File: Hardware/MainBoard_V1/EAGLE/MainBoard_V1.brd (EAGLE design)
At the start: 85 x 50 mm, 25 parts, among them IC1 REG1117, J1 NANO_FOOTPRINTNANO, J4 I2C, K1 RELAY-SPDT-JZC-11F, Q2 600mA/40V, Q3 600mA/40V, U1 MOC3021M, U2 TXB0104, U4 MCT2EM, X2 AC

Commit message: SubBoard_V1 initial state
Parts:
- removed U2: TXB0104, SparkFun-IC-Comms:SO14
- added JP1: (no value), SparkFun-Jumpers:SMT-JUMPER_2_NO_SILK
- added U$1, U$2, U$3, U$4, U$5, U$6, U$7, U$8: FIDUCIAL, adafruit:FIDUCIAL_1MM
- added U3: (no value), adafruit:VFSOP-8
- D2: value 1A/50V/1.1V -> S1M; device SparkFun-DiscreteSemi:DIODE-1N4001 -> diode:SMA
- R1, R3, R4, R5, R6: device rcl:R0402 -> rcl:R0603
- moved R6 9.27 mm to (34.0, 47.1)
- moved Q3 8.00 mm to (37.0, 46.0)
- moved Q2 7.52 mm to (37.0, 47.0)
- moved D2 5.71 mm to (43.7, 47.2), turned to 180 degrees
- moved R5 3.50 mm to (39.5, 45.9), turned to 270 degrees
- moved R4 2.43 mm to (31.9, 37.0), flipped to the bottom, turned to 90 degrees
- moved R1 1.26 mm to (68.0, 38.0)
- moved R3 1.14 mm to (34.0, 37.0), turned to 90 degrees
- moved C1 1.08 mm to (53.0, 32.0)
- moved K1 1.00 mm to (58.0, 43.5)
- moved U1 0.40 mm to (40.0, 38.5)
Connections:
- net 3V3: now also U3.P$3, U3.P$6; no longer U2.1, U2.8
- net 5V: now also JP1.2, U3.P$7; no longer U2.14
- net A4: now also U3.P$1; no longer U2.11
- net A5: now also U3.P$8; no longer U2.10
- net GND: now also U3.P$2; no longer U2.7
- net SCL: now also U3.P$5; no longer U2.5
- net SDA: now also U3.P$4; no longer U2.4
- net VIN: now also JP1.1
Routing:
- net GND: track 168.1 -> 122.3 mm, vias 2 -> 16
- net D9: track 50.3 -> 58.0 mm
- net SDA: track 30.5 -> 24.1 mm
- net PUMP: track 73.5 -> 79.9 mm
- net 5V: track 56.8 -> 51.0 mm
- net N$9: track 22.9 -> 17.4 mm, vias 0 -> 1
- net D10: track 65.3 -> 60.2 mm, vias 3 -> 1
- net SCL: track 30.6 -> 26.2 mm
- net 3V3: track 61.2 -> 57.2 mm, vias 2 -> 1
- net N$10: track 5.40 -> 1.71 mm
- net A5: track 8.19 -> 5.43 mm
- net N$1: track 31.1 -> 33.4 mm
- net VIN: track 53.2 -> 55.4 mm
- net 3WAYVALVE: track 21.4 -> 19.3 mm
- net ACPOS: track 37.3 -> 35.3 mm, vias 1 -> 0
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- added copper zone on layer 1, net GND
- removed copper zone on layer 1, net 3V3
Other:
- board text added: "3 P N L"

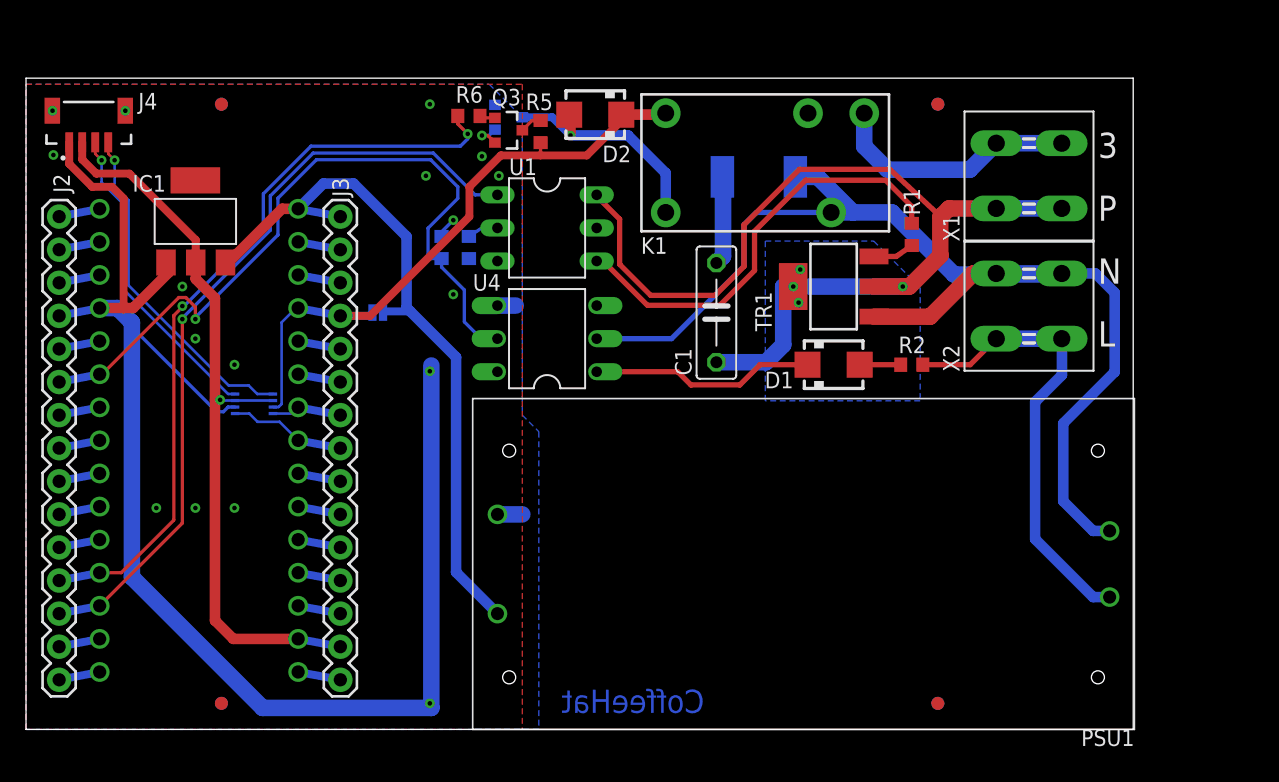
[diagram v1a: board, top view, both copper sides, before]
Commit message: Mounting holes
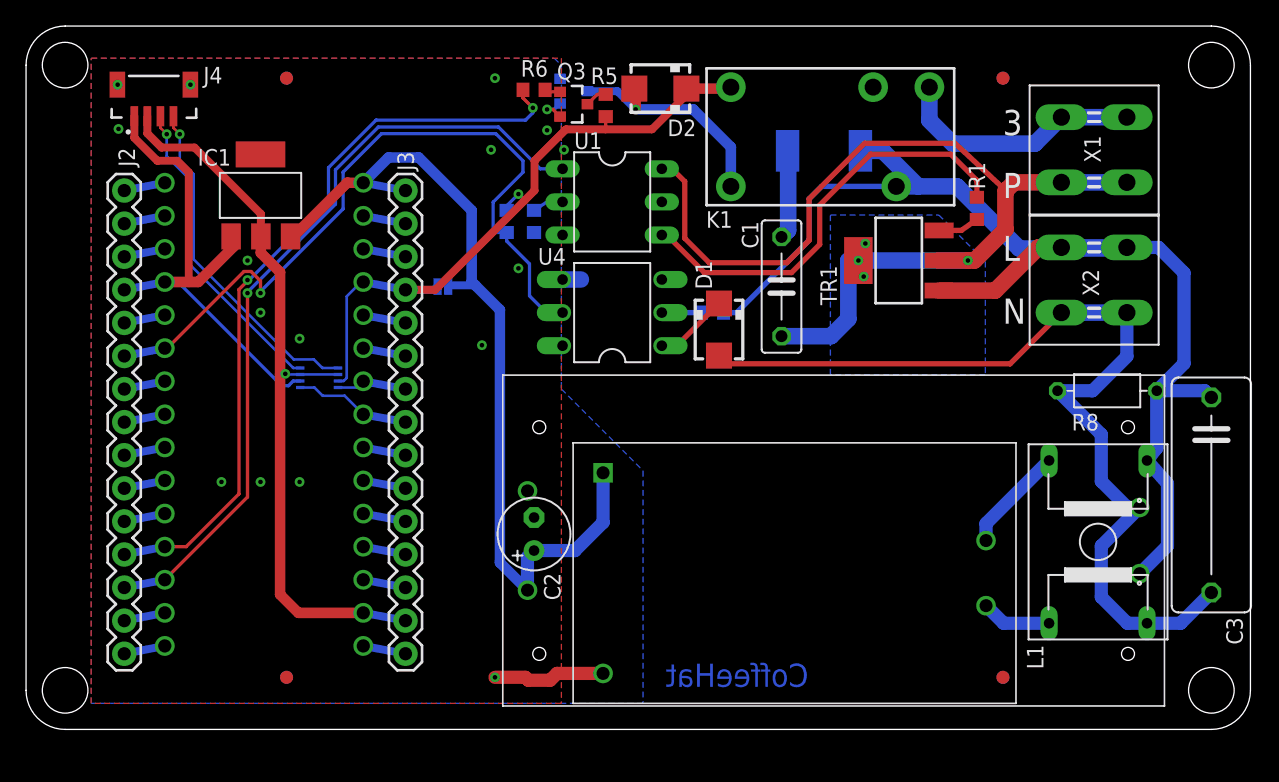
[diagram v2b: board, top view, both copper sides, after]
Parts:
- added C2: 220uF, rcl:E2,5-6
- added C3: (no value), rcl:C150-064X183
- added L1: DFKH14, inductors:DFKH14
- added PSU2: HLK-10M05, discrete:HLK-10MXX
- added R8: VARISTOR-7,5, varistor:R-7,5
- moved R2 15.8 mm to (52.7, 32.0), flipped to the bottom, turned to 180 degrees
- moved D1 9.20 mm to (53.2, 30.7), turned to 270 degrees
- moved C1 5.39 mm to (58.0, 34.0)
- moved D2 5.39 mm to (48.7, 49.2)
- moved IC1 5.39 mm to (18.0, 41.0)
- moved J1 5.39 mm to (18.3, 24.2)
- moved J2 5.39 mm to (7.54, 41.4)
- moved JP1 5.39 mm to (32.0, 34.0)
- moved K1 5.39 mm to (63.0, 45.5)
- moved Q2 5.39 mm to (42.0, 49.0)
- moved Q3 5.39 mm to (42.0, 48.0)
- moved R1 5.39 mm to (73.0, 40.0)
- moved R3 5.39 mm to (39.0, 39.0)
- moved R4 5.39 mm to (36.9, 39.0)
- moved R5 5.39 mm to (44.5, 47.9)
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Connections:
- removed net ACNEG: K1.4, PSU1.AC_N, R7.1, TR1.1, U4.2, X2.3, X2.4
- removed net ACPOS: PSU1.AC_L, R2.2, X2.1, X2.2
- new net ACL: C3.1, K1.4, L1.1, PSU1.AC_L, R2.2, R7.1, R8.1, TR1.1, X2.3, X2.4
- new net ACN: C3.2, D1.A, L1.4, PSU1.AC_N, R8.2, X2.1, X2.2
- new net N$12: L1.3, PSU2.AC1
- new net N$7: L1.2, PSU2.AC2
- net GND: now also C2.-, PSU2.V-
- net N$5: now also U4.2; no longer D1.A
- net VIN: now also C2.+, PSU2.V+
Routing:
- net ACL: track 0.00 -> 95.5 mm
- net ACNEG: track 91.8 -> 0.00 mm
- net ACN: track 0.00 -> 73.5 mm
- net GND: track 122.3 -> 53.1 mm
- net ACPOS: track 35.3 -> 0.00 mm
- net VIN: track 55.4 -> 67.7 mm
- net N$6: track 17.3 -> 5.73 mm
- net N$7: track 0.00 -> 8.15 mm
- net N$12: track 0.00 -> 5.40 mm
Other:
- board size 85 x 50 mm -> 94 x 54 mm
- board text added: "3 P L N"
- board text removed: "3 P N L"

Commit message: All SMD to the top layer
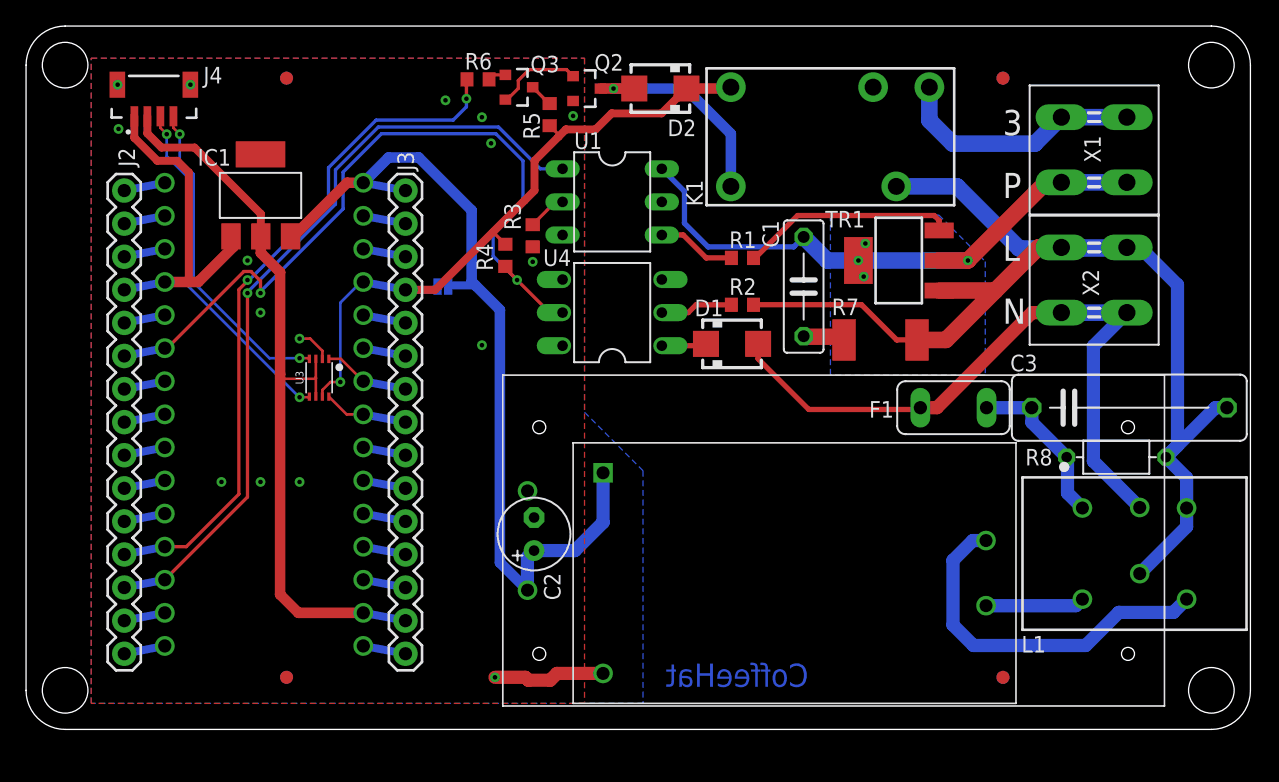
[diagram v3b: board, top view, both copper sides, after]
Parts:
- added F1: (no value), fuse:TE5
- C3: value (none) -> 0.1uF; device rcl:C150-064X183 -> rcl:C150-054X183
- L1: value DFKH14 -> 18mH; device inductors:DFKH14 -> Wurth_EMC Components_WE-TFC:WE-TFC_UU9.8V
- R8: value VARISTOR-7,5 -> (none)
- moved R1 18.4 mm to (55.0, 36.2), turned to 0 degrees
- moved R7 15.2 mm to (65.6, 29.9), flipped to the top, turned to 180 degrees
- moved C3 9.20 mm to (84.7, 24.7), turned to 0 degrees
- moved R8 5.15 mm to (83.7, 20.9), turned to 0 degrees
- moved Q3 4.40 mm to (37.8, 49.3)
- moved R6 4.37 mm to (34.7, 49.9)
- moved R5 4.36 mm to (40.2, 47.2)
- moved L1 2.94 mm to (85.1, 13.5), turned to 0 degrees
- moved R4 2.60 mm to (36.8, 36.4), flipped to the top
- moved R2 2.38 mm to (55.0, 32.6), flipped to the top, turned to 0 degrees
- moved C1 1.70 mm to (59.7, 34.0), turned to 270 degrees
- moved D1 1.49 mm to (54.2, 29.6), turned to 0 degrees
- moved R3 1.10 mm to (38.9, 37.9), flipped to the top
- moved Q2 1.02 mm to (43.0, 49.2), flipped to the top, turned to 270 degrees
- flipped U3 to the top, turned to 180 degrees
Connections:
- new net ACN1: C3.1, F1.2, L1.1, R8.1
- net A4: now also U3.P$8; no longer U3.P$1
- net A5: now also U3.P$1; no longer U3.P$8
- net ACL: now also C3.2, L1.2, R8.2; no longer C3.1, L1.1, R8.1
- net ACN: now also F1.1; no longer C3.2, L1.4, R8.2
- net N$12: now also PSU2.AC2; no longer PSU2.AC1
- net N$7: now also L1.4, PSU2.AC1; no longer L1.2, PSU2.AC2
- net SCL: now also U3.P$4; no longer U3.P$5
- net SDA: now also U3.P$5; no longer U3.P$4
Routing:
- net PUMP: track 80.0 -> 48.3 mm
- net N$1: track 33.1 -> 6.07 mm
- net N$12: track 5.40 -> 28.2 mm
- net ACN: track 73.5 -> 51.7 mm
- net N$2: track 3.17 -> 16.5 mm
- net ACN1: track 0.00 -> 12.8 mm
- net GND: track 53.1 -> 40.6 mm
- net D9: track 58.0 -> 53.2 mm
- net N$8: track 2.41 -> 6.72 mm, vias 1 -> 0
- net N$4: track 6.84 -> 3.22 mm
- net SDA: track 24.1 -> 26.8 mm, vias 1 -> 2
- net ACL: track 95.5 -> 92.8 mm
- net N$5: track 3.04 -> 5.59 mm
- net A4: track 8.99 -> 6.55 mm
- net N$6: track 5.73 -> 3.45 mm
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
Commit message: Warning symbols added
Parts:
- added U$9: (no value), discrete:HV_LOGO_3
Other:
- board text added: "DANGER! HIGH VOLTAGE!"
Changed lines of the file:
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@@
 <drawing>
 <settings>
-<setting alwaysvectorfont="yes"/>
+<setting alwaysvectorfont="no"/>
 <setting verticaltext="up"/>
 </settings>
@@
 <wire x1="91" y1="54" x2="94" y2="51" width="0" layer="20" curve="-90"/>
 <wire x1="94" y1="3" x2="91" y2="0" width="0" layer="20" curve="-90"/>
+<wire x1="86.36" y1="52.07" x2="64.77" y2="52.07" width="0.3048" layer="22" style="shortdash"/>
+<wire x1="64.77" y1="52.07" x2="62.23" y2="49.53" width="0.3048" layer="22" style="shortdash"/>
+<wire x1="62.23" y1="49.53" x2="62.23" y2="43.18" width="0.3048" layer="22" style="shortdash"/>
+<wire x1="62.23" y1="43.18" x2="58.42" y2="39.37" width="0.3048" layer="22" style="shortdash"/>
+<wire x1="58.42" y1="39.37" x2="53.34" y2="39.37" width="0.3048" layer="22" style="shortdash"/>
+<wire x1="53.34" y1="39.37" x2="50.8" y2="41.91" width="0.3048" layer="22" style="shortdash"/>
+<wire x1="50.8" y1="41.91" x2="50.8" y2="43.18" width="0.3048" layer="22" style="shortdash"/>
+<wire x1="50.8" y1="43.18" x2="49.53" y2="44.45" width="0.3048" layer="22" style="shortdash"/>
+<wire x1="49.53" y1="44.45" x2="46.99" y2="44.45" width="0.3048" layer="22" style="shortdash"/>
+<wire x1="46.99" y1="44.45" x2="45.72" y2="43.18" width="0.3048" layer="22" style="shortdash"/>
+<wire x1="45.72" y1="43.18" x2="45.72" y2="29.21" width="0.3048" layer="22" style="shortdash"/>
+<wire x1="45.72" y1="29.21" x2="58.42" y2="16.51" width="0.3048" layer="22" style="shortdash"/>
+<wire x1="58.42" y1="16.51" x2="58.42" y2="8.89" width="0.3048" layer="22" style="shortdash"/>
+<wire x1="58.42" y1="8.89" x2="64.77" y2="2.54" width="0.3048" layer="22" style="shortdash"/>
+<wire x1="64.77" y1="2.54" x2="86.36" y2="2.54" width="0.3048" layer="22" style="shortdash"/>
+<wire x1="86.36" y1="2.54" x2="92.71" y2="8.89" width="0.3048" layer="22" style="shortdash"/>
+<wire x1="92.71" y1="8.89" x2="92.71" y2="45.72" width="0.3048" layer="22" style="shortdash"/>
+<wire x1="92.71" y1="45.72" x2="86.36" y2="52.07" width="0.3048" layer="22" style="shortdash"/>
+<text x="61.214" y="5.969" size="1.6764" layer="22" rot="MR0" align="bottom-right">DANGER!
+HIGH VOLTAGE!</text>
 </plain>
 <attributes>
@@
 <attribute name="VALUE" x="66.882" y="20.89" size="1.27" layer="27" ratio="10"/>
 </element>
+<element name="U$9" library="discrete" package="HV_LOGO_3" value="" x="80.01" y="10.668" smashed="yes" rot="MR0"/>
 </elements>
 <signals>
@@
 packages will not be understood (or retained) with this version.
 </note>
+<note version="8.5" severity="warning">
+Since Version 8.5, EAGLE supports locking for holes, vias, wires and polygons.
+The locking property on all objects of these types will not be understood in this version.
+</note>
 </compatibility>

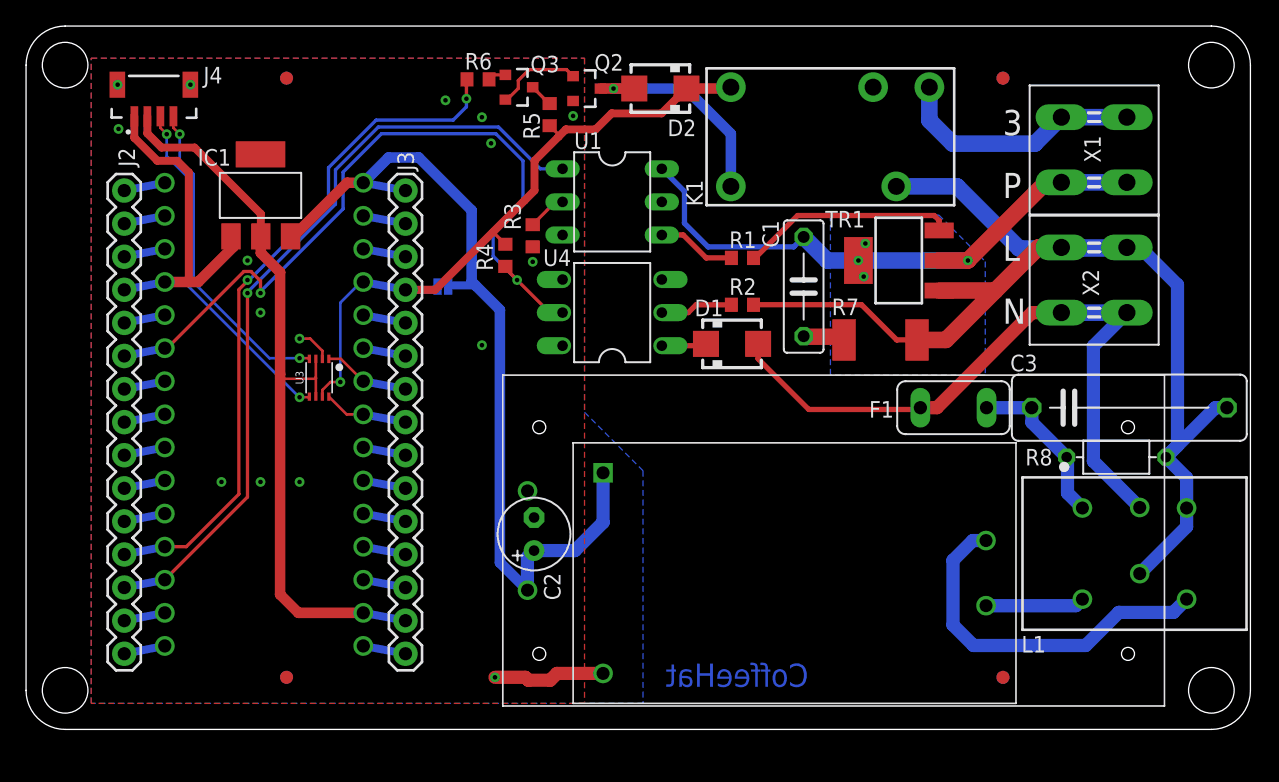
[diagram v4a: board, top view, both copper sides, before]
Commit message: I2C pullups
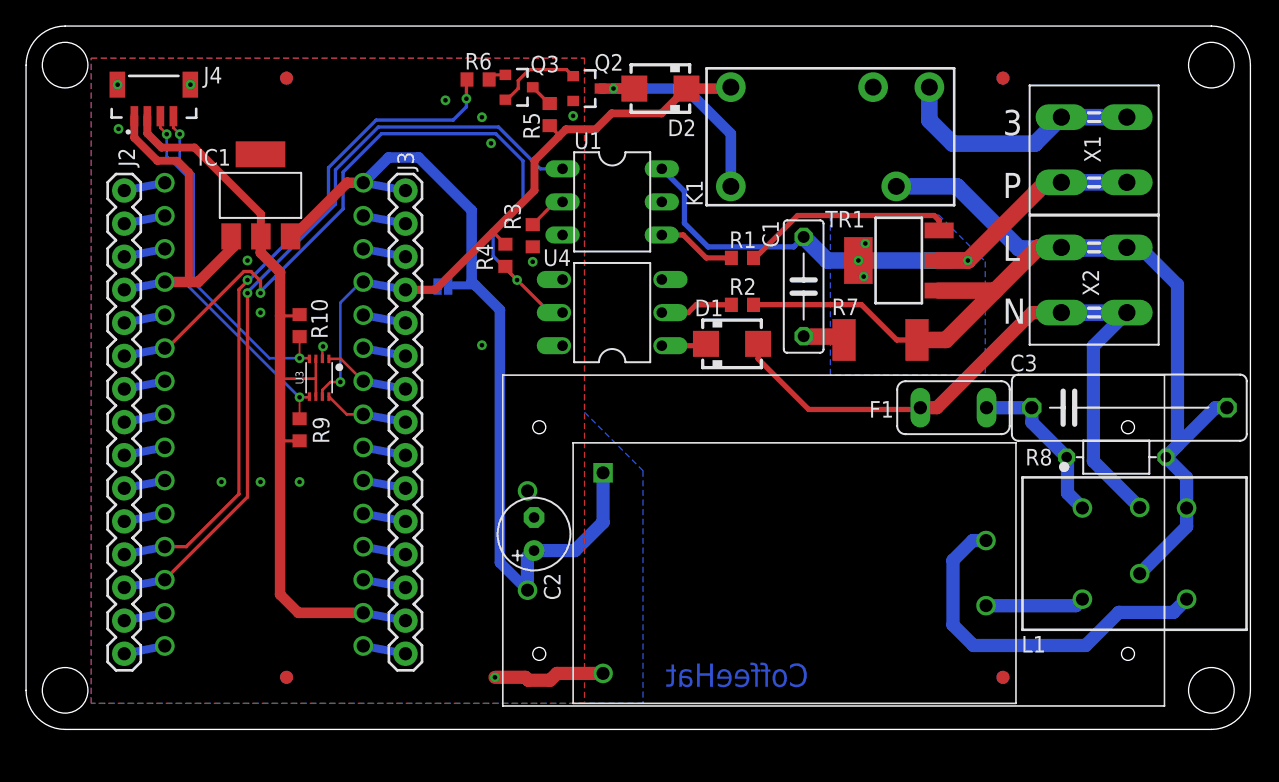
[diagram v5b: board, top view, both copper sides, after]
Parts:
- added R10, R9: 10K, rcl:R0603
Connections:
- net 3V3: now also R10.2, R9.2
- net SCL: now also R10.1
- net SDA: now also R9.1
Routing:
- net 3V3: track 58.4 -> 61.3 mm
- net GND: track 40.6 -> 38.8 mm
- net SDA: track 26.8 -> 28.5 mm
- net SCL: track 24.7 -> 26.4 mm
